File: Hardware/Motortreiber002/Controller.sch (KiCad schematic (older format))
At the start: 1 part, among them U5 ATmega64-16AU

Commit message: Umbau auf ATXMega128 Start
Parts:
- removed U5: ATmega64-16AU, Package_QFP:TQFP-64_14x14mm_P0.8mm, symbol MCU_Microchip_ATmega:ATmega64-16AU
- added U?: ADUM3160, Package_SO:SOIC-16W_7.5x10.3mm_P1.27mm, symbol Interface_USB:ADUM3160
- added U?: ATxmega128C3-AU, Package_QFP:TQFP-64_14x14mm_P0.8mm, symbol MCU_Microchip_ATmega:ATxmega128C3-AU
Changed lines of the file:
@@
 Text HLabel 6200 2700 2    50   Output ~ 0
 Uebernahme4
-$Comp
-L MCU_Microchip_ATmega:ATmega64-16AU U5
-U 1 1 5CB2CDF3
-P 5600 3700
-F 0 "U5" H 5600 1611 50  0000 C CNN
-F 1 "ATmega64-16AU" H 5600 1520 50  0000 C CNN
-F 2 "Package_QFP:TQFP-64_14x14mm_P0.8mm" H 5600 3700 50  0001 C CIN
-F 3 "http://ww1.microchip.com/downloads/en/DeviceDoc/atmel-2490-8-bit-avr-microcontroller-atmega64-l_datasheet.pdf" H 5600 3700 50  0001 C CNN
-	1    5600 3700
-	1    0    0    -1
-$EndComp
 Text HLabel 6200 2300 2    50   Output ~ 0
 CS4
@@
 Text HLabel 6200 2000 2    50   Output ~ 0
 CS1
+$Comp
+L Interface_USB:ADUM3160 U?
+U 1 1 5CBAA042
+P 1300 1450
+F 0 "U?" H 1300 2231 50  0000 C CNN
+F 1 "ADUM3160" H 1300 2140 50  0000 C CNN
+F 2 "Package_SO:SOIC-16W_7.5x10.3mm_P1.27mm" H 1300 750 50  0001 C CNN
+F 3 "https://www.analog.com/media/en/technical-documentation/data-sheets/ADuM3160.pdf" H 1100 1450 50  0001 C CNN
+	1    1300 1450
+	1    0    0    -1
+$EndComp
+$Comp
+L MCU_Microchip_ATmega:ATxmega128C3-AU U?
+U 1 1 5CBAF1B3
+P 4400 2550
+F 0 "U?" H 4400 661 50  0000 C CNN
+F 1 "ATxmega128C3-AU" H 4400 570 50  0000 C CNN
+F 2 "Package_QFP:TQFP-64_14x14mm_P0.8mm" H 4400 2550 50  0001 C CIN
+F 3 "http://ww1.microchip.com/downloads/en/DeviceDoc/Atmel-8492-8-and-16-bit-AVR-microcontroller-ATxmega32C3_64C3_128C3_192C3_256C3_datasheet.pdf" H 4400 2550 50  0001 C CNN
+	1    4400 2550
+	1    0    0    -1
+$EndComp
 $EndSCHEMATC

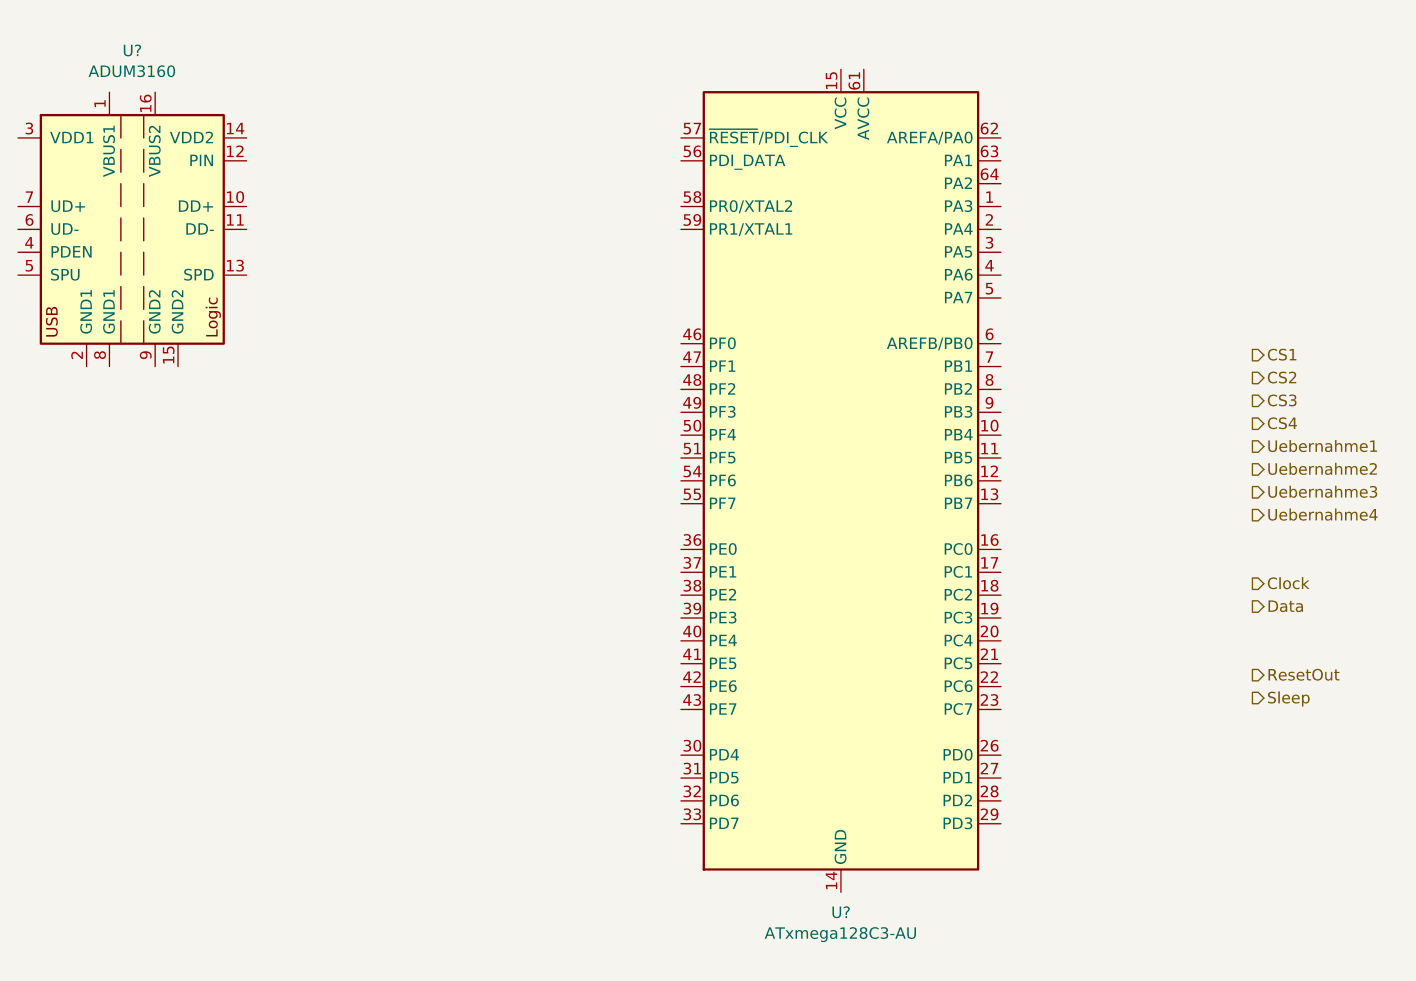
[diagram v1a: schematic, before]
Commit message: 16 Motortreiber 1 ATXMega 128 mit USB USB Anschluss noch nicht fertig
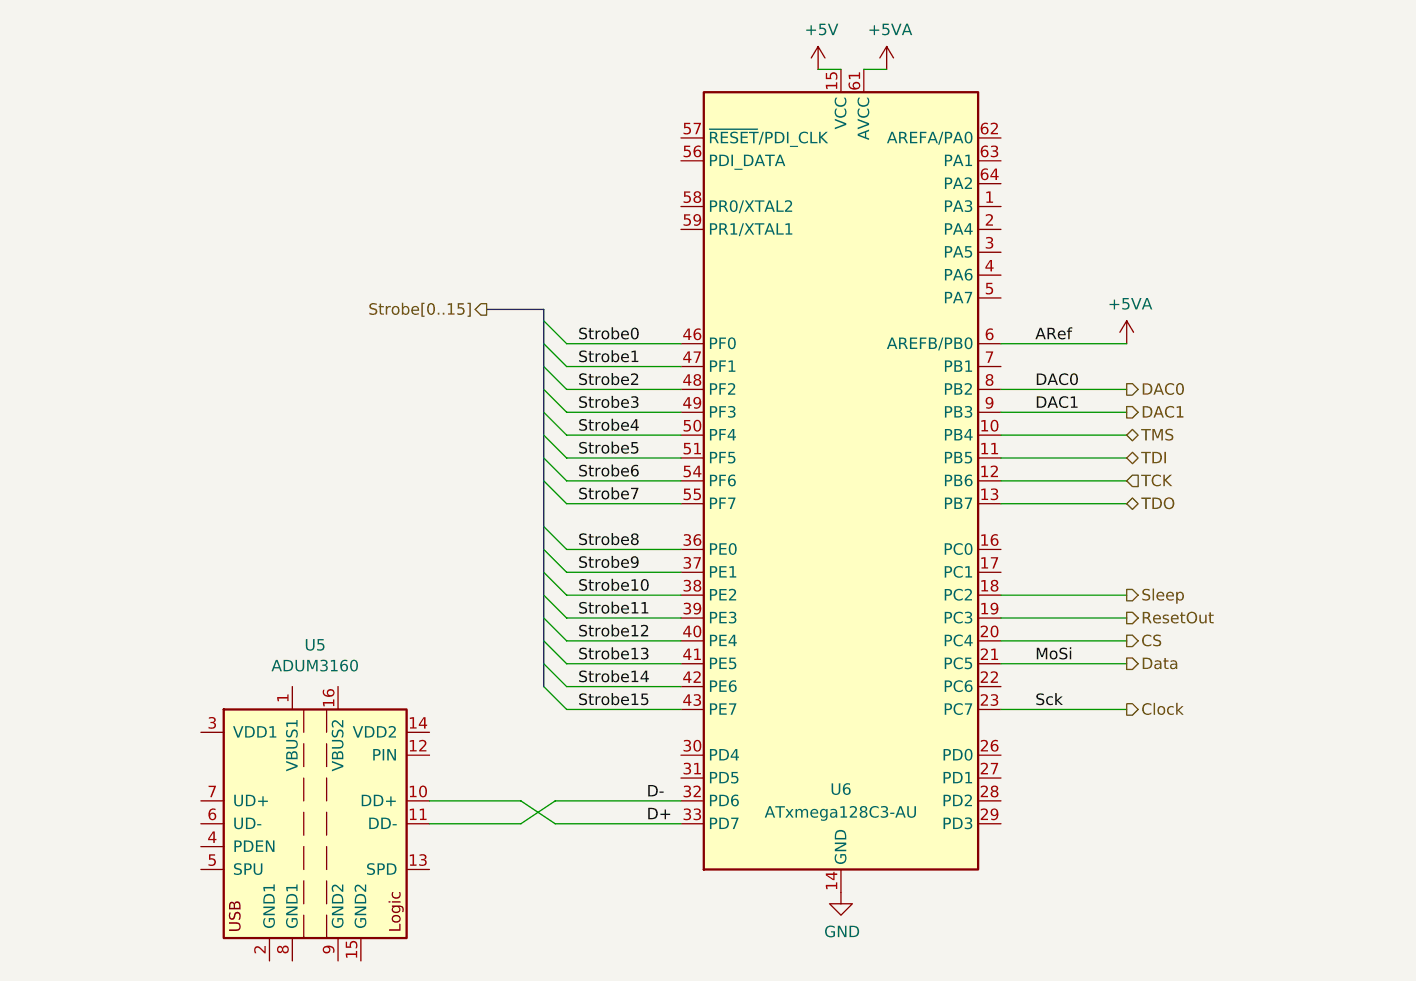
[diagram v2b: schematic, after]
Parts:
- gave numbers to parts that had none: 2
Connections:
- net Clock: now also U6.23 (PC7)
- net Data: now also U6.21 (PC5)
- net ResetOut: now also U6.19 (PC3)
- net Sleep: now also U6.18 (PC2)
- net D+: now reaches U5.10 (DD+)
- net D+: now also U6.33 (PD7)
- net D-: now reaches U5.11 (DD-)
- net D-: now also U6.32 (PD6)
- net TMS: now reaches U6.10 (PB4)
- net TDI: now reaches U6.11 (PB5)
- net TCK: now reaches U6.12 (PB6)
- net TDO: now reaches U6.13 (PB7)
- net GND: now reaches U6.14 (GND), U6.24 (GND), U6.34 (GND), U6.44 (GND), U6.52 (GND), U6.60 (GND)
- net +5V: now reaches U6.15 (VCC), U6.25 (VCC), U6.35 (VCC), U6.45 (VCC), U6.53 (VCC)
- net CS: now reaches U6.20 (PC4)
- net Strobe8: now reaches U6.36 (PE0)
- net Strobe9: now reaches U6.37 (PE1)
- net Strobe10: now reaches U6.38 (PE2)
- net Strobe11: now reaches U6.39 (PE3)
- net Strobe12: now reaches U6.40 (PE4)
- net Strobe13: now reaches U6.41 (PE5)
- net Strobe14: now reaches U6.42 (PE6)
- net Strobe15: now reaches U6.43 (PE7)
- net Strobe0: now reaches U6.46 (PF0)
- net Strobe1: now reaches U6.47 (PF1)
- net Strobe2: now reaches U6.48 (PF2)
- net Strobe3: now reaches U6.49 (PF3)
- net Strobe4: now reaches U6.50 (PF4)
- net Strobe5: now reaches U6.51 (PF5)
- net Strobe6: now reaches U6.54 (PF6)
- net Strobe7: now reaches U6.55 (PF7)
- net +5VA: now reaches U6.6 (AREFB/PB0)
- net +5VA: now also U6.61 (AVCC)
- net DAC0: now reaches U6.8 (PB2)
- net DAC1: now reaches U6.9 (PB3)
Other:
- moved on the sheet: U5

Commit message: Annotation auf Seiten bezogen
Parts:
- renumbered U5 to U501, U6 to U502
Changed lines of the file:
@@
 CS
 $Comp
-L Interface_USB:ADUM3160 U5
+L Interface_USB:ADUM3160 U501
 U 1 1 5CBAA042
 P 2100 4050
-F 0 "U5" H 2100 4831 50  0000 C CNN
+F 0 "U501" H 2100 4831 50  0000 C CNN
 F 1 "ADUM3160" H 2100 4740 50  0000 C CNN
 F 2 "Package_SO:SOIC-16W_7.5x10.3mm_P1.27mm" H 2100 3350 50  0001 C CNN
@@
 $EndComp
 $Comp
-L MCU_Microchip_ATmega:ATxmega128C3-AU U6
+L MCU_Microchip_ATmega:ATxmega128C3-AU U502
 U 1 1 5CBAF1B3
 P 4400 2550
-F 0 "U6" H 4400 1200 50  0000 C CNN
+F 0 "U502" H 4400 1200 50  0000 C CNN
 F 1 "ATxmega128C3-AU" H 4400 1100 50  0000 C CNN
 F 2 "Package_QFP:TQFP-64_14x14mm_P0.8mm" H 4400 2550 50  0001 C CIN
@@
 DAC1
 $Comp
-L power:+5V #PWR057
+L power:+5V #PWR0501
 U 1 1 5CC9E9BA
 P 4300 750
-F 0 "#PWR057" H 4300 600 50  0001 C CNN
+F 0 "#PWR0501" H 4300 600 50  0001 C CNN
 F 1 "+5V" H 4315 923 50  0000 C CNN
 F 2 "" H 4300 750 50  0001 C CNN
@@
 $EndComp
 $Comp
-L power:+5VA #PWR059
+L power:+5VA #PWR0503
 U 1 1 5CC9EE6C
 P 4600 750
-F 0 "#PWR059" H 4600 600 50  0001 C CNN
+F 0 "#PWR0503" H 4600 600 50  0001 C CNN
 F 1 "+5VA" H 4615 923 50  0000 C CNN
 F 2 "" H 4600 750 50  0001 C CNN
@@
 	3100 1800 3100 3450
 $Comp
-L power:+5VA #PWR060
+L power:+5VA #PWR0504
 U 1 1 5CCA0B35
 P 5650 1950
-F 0 "#PWR060" H 5650 1800 50  0001 C CNN
+F 0 "#PWR0504" H 5650 1800 50  0001 C CNN
 F 1 "+5VA" H 5665 2123 50  0000 C CNN
 F 2 "" H 5650 1950 50  0001 C CNN
@@
 $EndComp
 $Comp
-L power:GND #PWR058
+L power:GND #PWR0502
 U 1 1 5CCA0D2B
 P 4400 4350
-F 0 "#PWR058" H 4400 4100 50  0001 C CNN
+F 0 "#PWR0502" H 4400 4100 50  0001 C CNN
 F 1 "GND" H 4405 4177 50  0000 C CNN
 F 2 "" H 4400 4350 50  0001 C CNN
